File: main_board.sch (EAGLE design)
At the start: 99 parts, among them IC1 MBED_MICROCONTROLLER, M1_1 M01_WIRE, M1_10 M01_WIRE, M1_2 M01_WIRE, M1_3 M01_WIRE, M1_4 M01_WIRE, M1_5 M01_WIRE, M1_6 M01_WIRE, M1_7 M01_WIRE, M1_8 M01_WIRE, M1_9 M01_WIRE, U1 PCA9555PW,118, U11 MC33887-HSOP, U13 MC33887-HSOP, U2 SI8460AA-B-IS1, U3 MC33887-HSOP, U6 SI8460AA-B-IS1, U7 MC33887-HSOP, U8 SI8460AA-B-IS1, U9 MC33887-HSOP, X1 BALL_SENS, X10 IMU, X2 ETH, X3 ENC1, X4 ENC2, X5 BTNS, X6 ENC3, X7 ENC4, X8 ENC5, X9 COIL

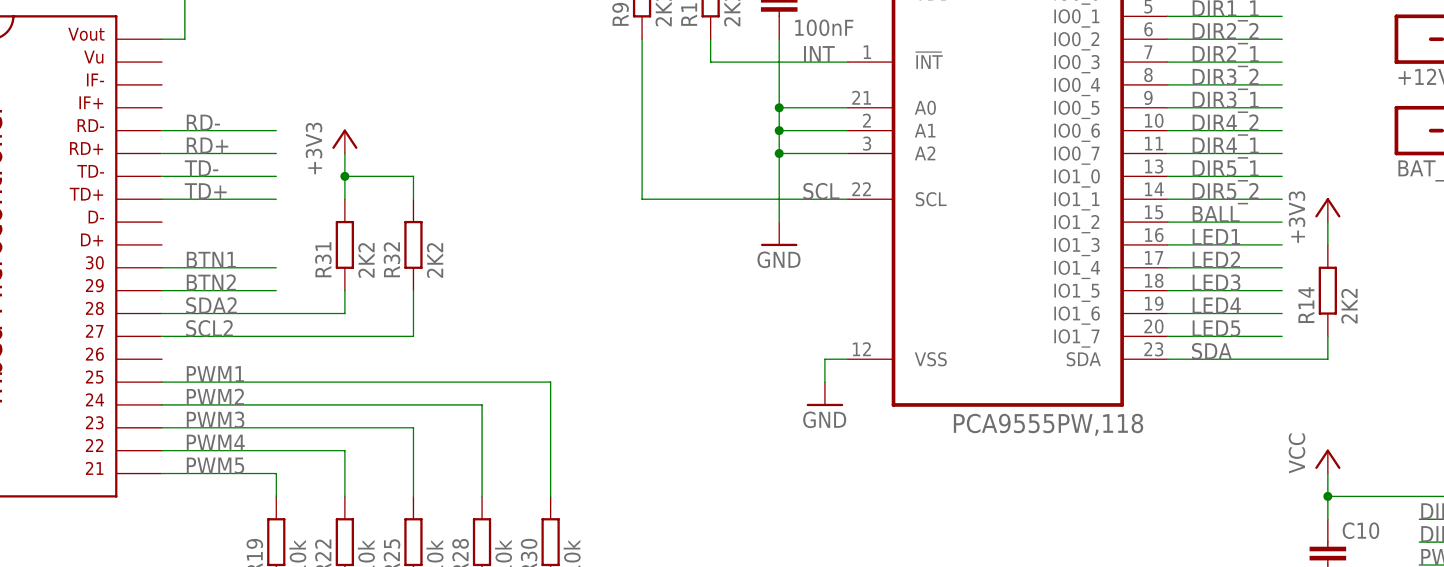
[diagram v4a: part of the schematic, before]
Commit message: Connected ball detector directly to mbed
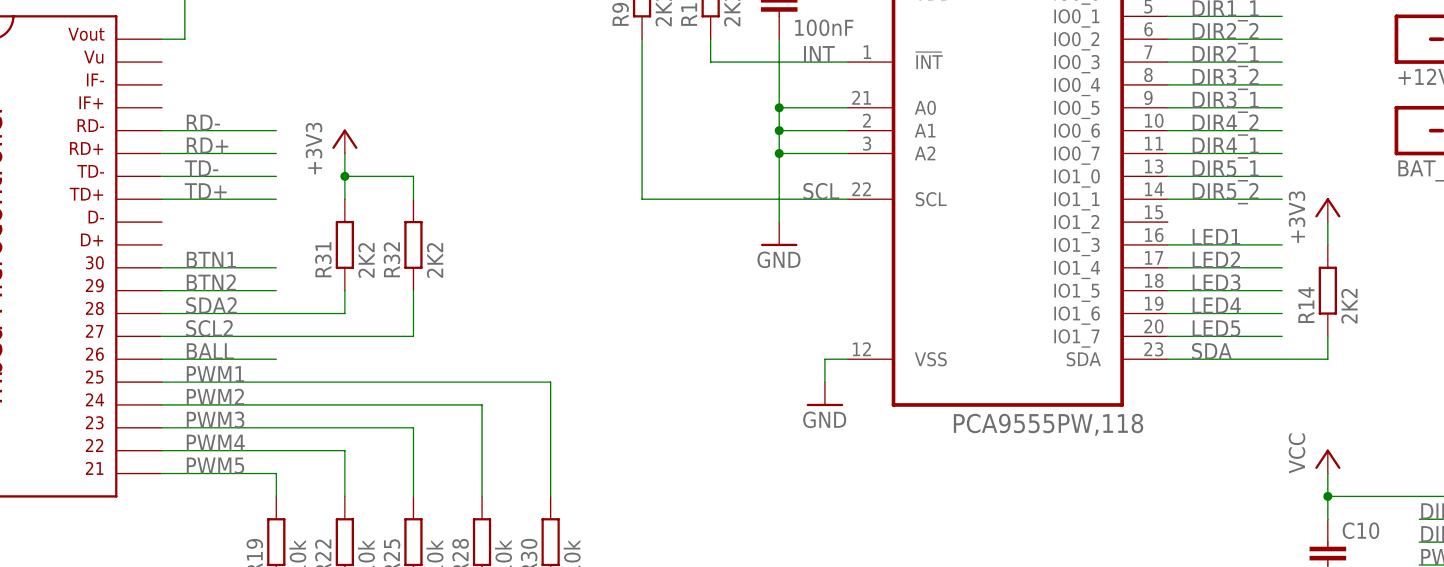
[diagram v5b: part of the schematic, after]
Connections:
- net BALL: now also IC1.P$26; no longer U1.IO1_2
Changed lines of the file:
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@@
 <?xml version="1.0" encoding="utf-8"?>
 <!DOCTYPE eagle SYSTEM "eagle.dtd">
-<eagle version="6.5.0">
+<eagle version="6.4">
 <drawing>
 <settings>
@@
 </segment>
 <segment>
-<pinref part="U1" gate="A" pin="IO1_2"/>
-<wire x1="91.44" y1="101.6" x2="104.14" y2="101.6" width="0.1524" layer="91"/>
-<label x="93.98" y="101.6" size="1.778" layer="95"/>
-</segment>
-</net>
+<pinref part="IC1" gate="G$1" pin="P$26"/>
+<wire x1="-20.32" y1="86.36" x2="-7.62" y2="86.36" width="0.1524" layer="91"/>
+<label x="-17.78" y="86.36" size="1.778" layer="95"/>
+</segment>
+</net>
